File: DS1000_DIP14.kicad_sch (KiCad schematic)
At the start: 2 parts

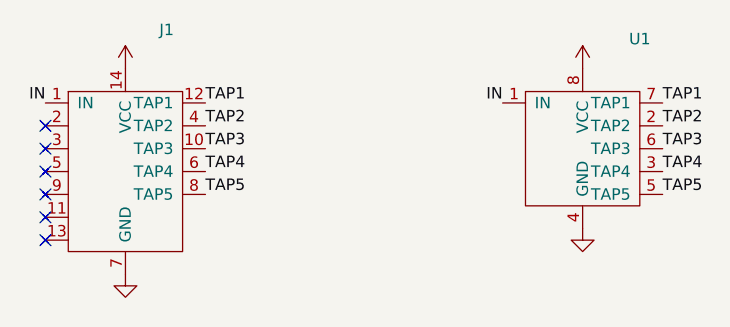
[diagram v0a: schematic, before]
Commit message: add SM8 DIP8, readme
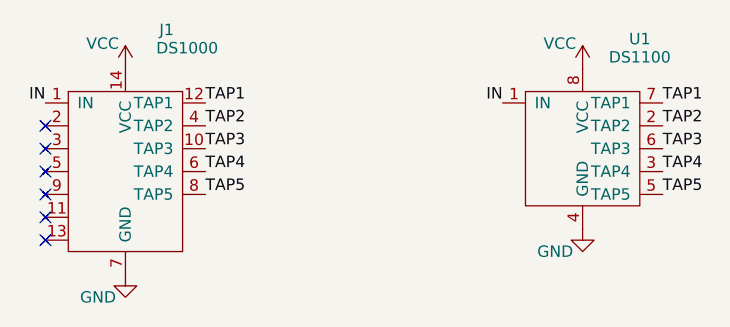
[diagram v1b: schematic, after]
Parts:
- J1: value (none) -> DS1000; footprint (none) -> 000_LOCAL:DIP14_0.3_pcb_sil_pins
- U1: value (none) -> DS1100; footprint (none) -> 000_LOCAL:SOIC-8_3.9x4.9mm_P1.27mm
